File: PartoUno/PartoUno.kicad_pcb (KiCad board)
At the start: 2 copper layers, 80 x 95.5 mm, 69 parts, among them J1 GNC_BOND, J10 RED5, J11 GRE3, J12 GRE2, J13 RED4, J14 GNC_BOND, J16 GNC_BOND, J17 GND_BOND, J18 GNC_BOND, J19 GNC_BOND, J2 WHI3, J20 TOP_STAR_VCC, J21 GNC_BOND, J23 GNC_BOND, J24 GNC_BOND, J25 GNC_BOND, J26 GNC_BOND, J28 GNC_BOND, J29 GNC_BOND, J3 YEL5, J30 GNC_BOND, J31 GNC_BOND, J32 GNC_BOND, J33 GNC_BOND, J34 GNC_BOND, J35 GNC_BOND, J4 BLU1, J5 BLU2, J6 YEL4, J7 WHI4, J8 YEL3, J9 GRE1, U1 ATtiny45V-10S, U2 74HC595, U3 74HC595, U4 74HC595

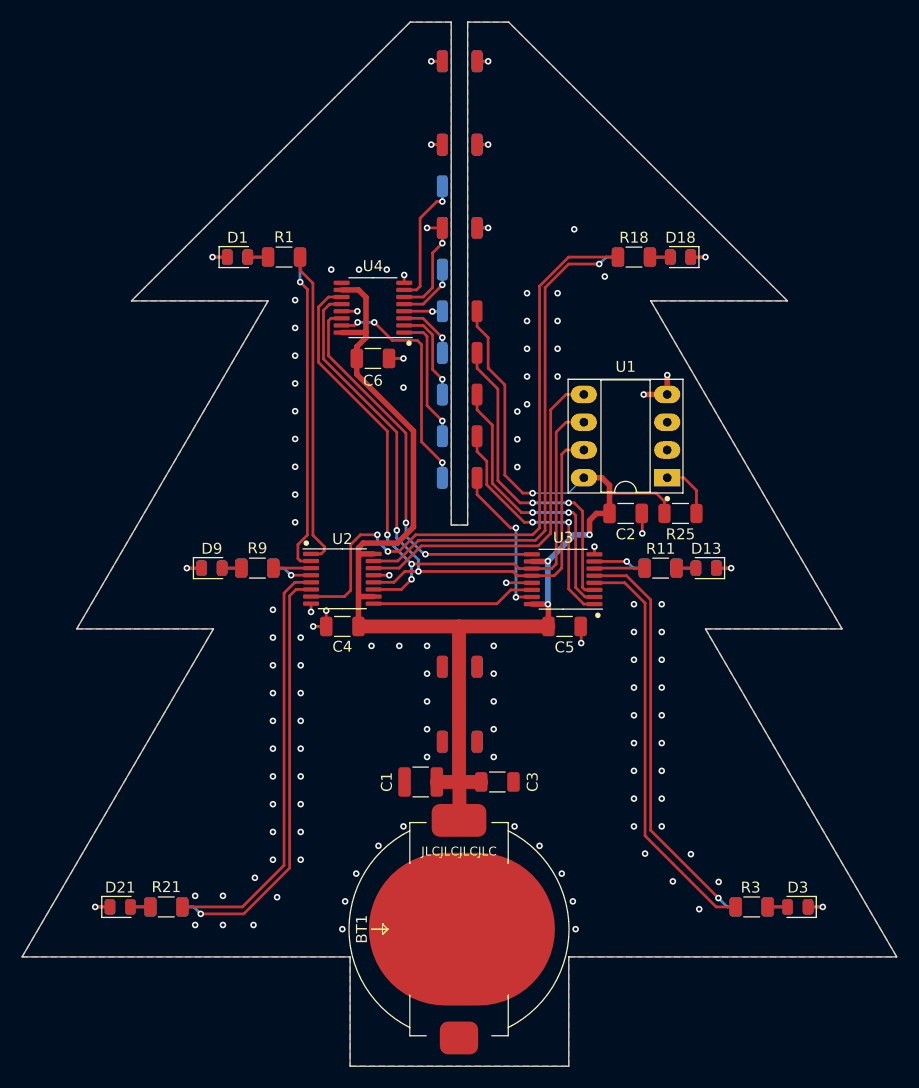
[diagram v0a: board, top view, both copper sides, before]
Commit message: Updated design
+ top LED
+ power switch
~ routing
~ via stitching more aligned
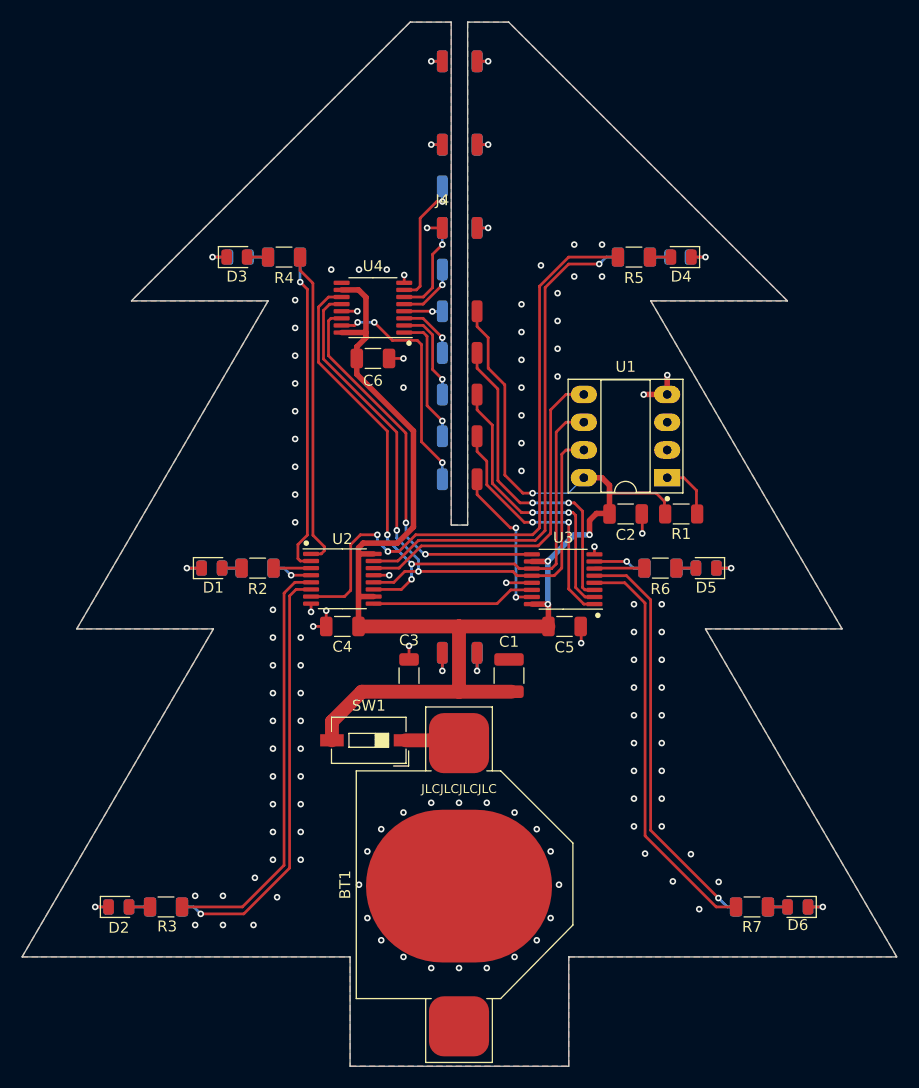
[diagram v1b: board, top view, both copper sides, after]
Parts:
- removed D13, D14: YEL, LED_SMD:LED_0805_2012Metric
- removed D18, D19, D20: BLU, LED_SMD:LED_0805_2012Metric
- removed D21, D22: WHI, LED_SMD:LED_0805_2012Metric
- removed J29, J30, J31, J32, J33, J34, J35: GNC_BOND, Connector_Wire:SolderWirePad_1x01_SMD_1x2mm
- removed R18, R19, R20, R21, R22: 1, Resistor_SMD:R_1206_3216Metric
- removed R25: 10k, Resistor_SMD:R_1206_3216Metric
- added D11: RED, LED_SMD:LED_0805_2012Metric, B.Cu at (163.1, 107.4)
- added D12: BLU, LED_SMD:LED_0805_2012Metric, B.Cu at (171.4, 138.4)
- added D4: BLU, LED_SMD:LED_0805_2012Metric, F.Cu at (160.8, 79.0)
- added D5: YEL, LED_SMD:LED_0805_2012Metric, F.Cu at (163.1, 107.4)
- added D6: RED, LED_SMD:LED_0805_2012Metric, F.Cu at (171.4, 138.4)
- added D7: YEL, LED_SMD:LED_0805_2012Metric, B.Cu at (120.3, 79.0)
- added D8: BLU, LED_SMD:LED_0805_2012Metric, B.Cu at (117.9, 107.4)
- added J15: GNC_BOND, Connector_Wire:SolderWirePad_1x01_SMD_1x2mm, B.Cu at (142.1, 61.1)
- added J22: GRE2, Connector_Wire:SolderWirePad_1x01_SMD_1x2mm, B.Cu at (138.9, 76.3)
- added J27: GRE3, Connector_Wire:SolderWirePad_1x01_SMD_1x2mm, B.Cu at (138.9, 99.3)
- added R13: 1, Resistor_SMD:R_1206_3216Metric, B.Cu at (167.3, 138.4)
- added R4: 51, Resistor_SMD:R_1206_3216Metric, F.Cu at (124.5, 79.0)
- added R5: 1, Resistor_SMD:R_1206_3216Metric, F.Cu at (156.5, 79.0)
- added R6: 39, Resistor_SMD:R_1206_3216Metric, F.Cu at (158.9, 107.4)
- added R7: 51, Resistor_SMD:R_1206_3216Metric, F.Cu at (167.3, 138.4)
- added R8: 39, Resistor_SMD:R_1206_3216Metric, B.Cu at (124.5, 79.0)
- added SW1: ON/OFF, Button_Switch_SMD:SW_DIP_SPSTx01_Slide_6.7x4.1mm_W6.73mm_P2.54mm_LowProfile_JPin, F.Cu at (132.2, 123.2)
- BT1: footprint custom:2032 battery narrow -> custom:2032 battery clip
- C2: value 0.47u -> 0.1u
- C3: value 0.1u -> 0.47u
- D1: value RED -> GRE
- D10: value GRE -> WHI
- D2: value RED -> WHI; moved to F.Cu
- D9, J14, J16: moved to B.Cu
- J1: value GNC_BOND -> RED4; moved to B.Cu
- J10: value RED5 -> YEL3
- J11: value GRE3 -> GRE1; moved to F.Cu
- J12: value GRE2 -> WHI3
- J13: value RED4 -> GNC_BOND
- J17: value GND_BOND -> GNC_BOND
- J2: value WHI3 -> YEL4
- J20: value TOP_STAR_VCC -> GNC_BOND
- J23: value GNC_BOND -> BLU2
- J24: value GNC_BOND -> YEL5
- J25: value GNC_BOND -> WHI4; moved to F.Cu
- J26: value GNC_BOND -> RED5; moved to F.Cu
- J28: value GNC_BOND -> TOP_STAR_VCC
- J3: value YEL5 -> BLU1
- J4: value BLU1 -> GNC_BOND; moved to F.Cu
- J5: value BLU2 -> GNC_BOND
- J6: value YEL4 -> GNC_BOND; moved to F.Cu
- J7: value WHI4 -> GNC_BOND
- J8: value YEL3 -> GNC_BOND
- J9: value GRE1 -> GNC_BOND; moved to B.Cu
- R1: value 51 -> 10k
- R11, R9: value 39 -> 1; moved to B.Cu
- R12: value 39 -> 51
- R2: value 51 -> 39; moved to F.Cu
- R3: value 51 -> 1
- moved D3 78.5 mm to (120.1, 79.0), turned to 0 degrees
- moved D10 78.4 mm to (160.7, 79.0), turned to 180 degrees
- moved D2 62.0 mm to (109.3, 138.4), turned to 0 degrees
- moved R3 53.6 mm to (113.7, 138.4), turned to 0 degrees
- moved R12 44.7 mm to (158.9, 107.4), turned to 180 degrees
- moved R1 43.3 mm to (160.8, 102.5), turned to 180 degrees
- moved J13 42.7 mm to (138.9, 115.2)
- moved R2 36.9 mm to (122.0, 107.4), turned to 0 degrees
- moved J28 32.7 mm to (142.1, 83.9)
- moved D9 32.1 mm to (109.3, 138.4)
- moved J20 31.2 mm to (142.1, 115.2)
- moved J24 30.6 mm to (138.9, 91.6)
- moved R11 28.6 mm to (156.5, 79.0)
- moved D1 28.5 mm to (117.9, 107.4)
- moved J8 27.6 mm to (138.9, 115.2)
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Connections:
- BT1 pad 1: VCC -> Net-(BT1-Pad1)
- J1 pad 1: GND -> /RED4
- J10 pad 1: /RED5 -> /YEL3
- J11 pad 1: /GRE3 -> /GRE1
- J12 pad 1: /GRE2 -> /WHI3
- J13 pad 1: /RED4 -> GND
- J2 pad 1: /WHI3 -> /YEL4
- J20 pad 1: VCC -> GND
- J23 pad 1: GND -> /BLU2
- J24 pad 1: GND -> /YEL5
- J25 pad 1: GND -> /WHI4
- J26 pad 1: GND -> /RED5
- J28 pad 1: GND -> VCC
- J3 pad 1: /YEL5 -> /BLU1
- J4 pad 1: /BLU1 -> GND
- J5 pad 1: /BLU2 -> GND
- J6 pad 1: /YEL4 -> GND
- J7 pad 1: /WHI4 -> GND
- J8 pad 1: /YEL3 -> GND
- J9 pad 1: /GRE1 -> GND
- R1 pad 1: Net-(D1-Pad2) -> Net-(R1-Pad1)
- R1 pad 2: /RED1 -> VCC
- R10 pad 1: Net-(D10-Pad2) -> Net-(D9-Pad2)
- R11 pad 1: Net-(D13-Pad2) -> Net-(D10-Pad2)
- R11 pad 2: /YEL1 -> /WHI2
- R12 pad 2: /YEL2 -> /RED2
- R2 pad 1: Net-(D2-Pad2) -> Net-(D1-Pad2)
- R2 pad 2: /RED2 -> /GRE4
- R3 pad 1: Net-(D3-Pad2) -> Net-(D2-Pad2)
- R3 pad 2: /RED3 -> /WHI1
- R9 pad 1: Net-(D9-Pad2) -> Net-(D8-Pad2)
- R9 pad 2: /GRE4 -> /BLU5
- U1 pad 1: Net-(R25-Pad1) -> Net-(R1-Pad1)
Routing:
- net GND: track 49.5 -> 57.4 mm, vias 123 -> 126
- net Net-(R25-Pad1): track 5.26 -> 0.00 mm
- net Net-(R1-Pad1): track 0.00 -> 5.26 mm
- net Net-(BT1-Pad1): track 0.00 -> 5.00 mm
- net VCC: track 135.9 -> 139.3 mm
- net Net-(D5-Pad2): track 0.00 -> 1.79 mm
- net Net-(D13-Pad2): track 1.79 -> 0.00 mm
- net Net-(D8-Pad2): track 0.00 -> 1.79 mm
- net Net-(D7-Pad2): track 0.00 -> 1.79 mm
- net Net-(D20-Pad2): track 1.79 -> 0.00 mm
- net Net-(D4-Pad2): track 0.00 -> 1.79 mm
- net Net-(D22-Pad2): track 1.79 -> 0.00 mm
- net Net-(D21-Pad2): track 1.79 -> 0.00 mm
- net Net-(D19-Pad2): track 1.79 -> 0.00 mm
- net Net-(D18-Pad2): track 1.79 -> 0.00 mm
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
